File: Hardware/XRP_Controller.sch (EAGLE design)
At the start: 121 parts, among them J1 POWER_JACKPOWER_JACK_SLOT, J12 Vertical Qwiic Connector, J13 Vertical Qwiic Connector, J14 Vertical Qwiic Connector, J3 JST_6_PIN_VERTICAL, J4 JST_6_PIN_VERTICAL, J5 JST_6_PIN_VERTICAL, J6 JST_6_PIN_VERTICAL, J9 Vertical Qwiic Connector, Q3 20V/4.2A/52mΩ/1.4W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

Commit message: Put all XRP specific parts into a single library
Helps ensure PROD_ID values are correct for this project
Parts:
- U1: value RPI_PICO_W -> RPI_PICO_W_XRP; device RPI_PICO_W:RPI_PICO_W -> XRP_COMPONENTS:RPI_PICO_W_XRP
- U4: value LSM6DS0 -> LSM6DS0X; device SparkFun-Sensors:LSM6DSO -> XRP_COMPONENTS:LSM6DSOX_XRP
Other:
- note added: "Cut VUSB jumper to prevent motors and servos from being powered by USB"
- note removed: "Open VUSB jumper to prevent motors and servos from being powered by USB"
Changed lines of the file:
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@@
 <part name="J8" library="SparkFun-Connectors" deviceset="CONN_03" device="LOCK_NO_SILK"/>
 <part name="J9" library="SparkFun-Connectors" deviceset="QWIIC_CONNECTOR" device="" value="Vertical Qwiic Connector"/>
-<part name="U4" library="SparkFun-Sensors" deviceset="LSM6DSO" device="" value="LSM6DS0"/>
+<part name="U4" library="XRP_COMPONENTS" deviceset="LSM6DSOX_XRP" device="" value="LSM6DS0X"/>
 <part name="U5" library="SparkFun-IC-Special-Function" deviceset="DRV883X" device="" value="DRV8835"/>
 <part name="U6" library="SparkFun-IC-Special-Function" deviceset="DRV883X" device="" value="DRV8835"/>
@@
 <part name="R19" library="SparkFun-Resistors" deviceset="10OHM" device="-1206-1/4W-1%" value="10"/>
 <part name="R18" library="SparkFun-Resistors" deviceset="10OHM" device="-1206-1/4W-1%" value="10"/>
-<part name="U1" library="RPI_PICO_W" deviceset="RPI_PICO_W" device=""/>
+<part name="U1" library="XRP_COMPONENTS" deviceset="RPI_PICO_W_XRP" device=""/>
 <part name="TP39" library="SparkFun-Connectors" deviceset="TEST-POINT" device="3X5"/>
 <part name="TP38" library="SparkFun-Connectors" deviceset="TEST-POINT" device="3X5"/>
@@
 <text x="20.32" y="172.72" size="2.54" layer="97" font="vector" align="center">Cut PWR jumper to
 remove power LED</text>
-<text x="45.72" y="93.98" size="2.54" layer="97" font="vector" align="center">Open VUSB jumper to
+<text x="45.72" y="93.98" size="2.54" layer="97" font="vector" align="center">Cut VUSB jumper to
 prevent motors and servos
 from being powered by USB</text>

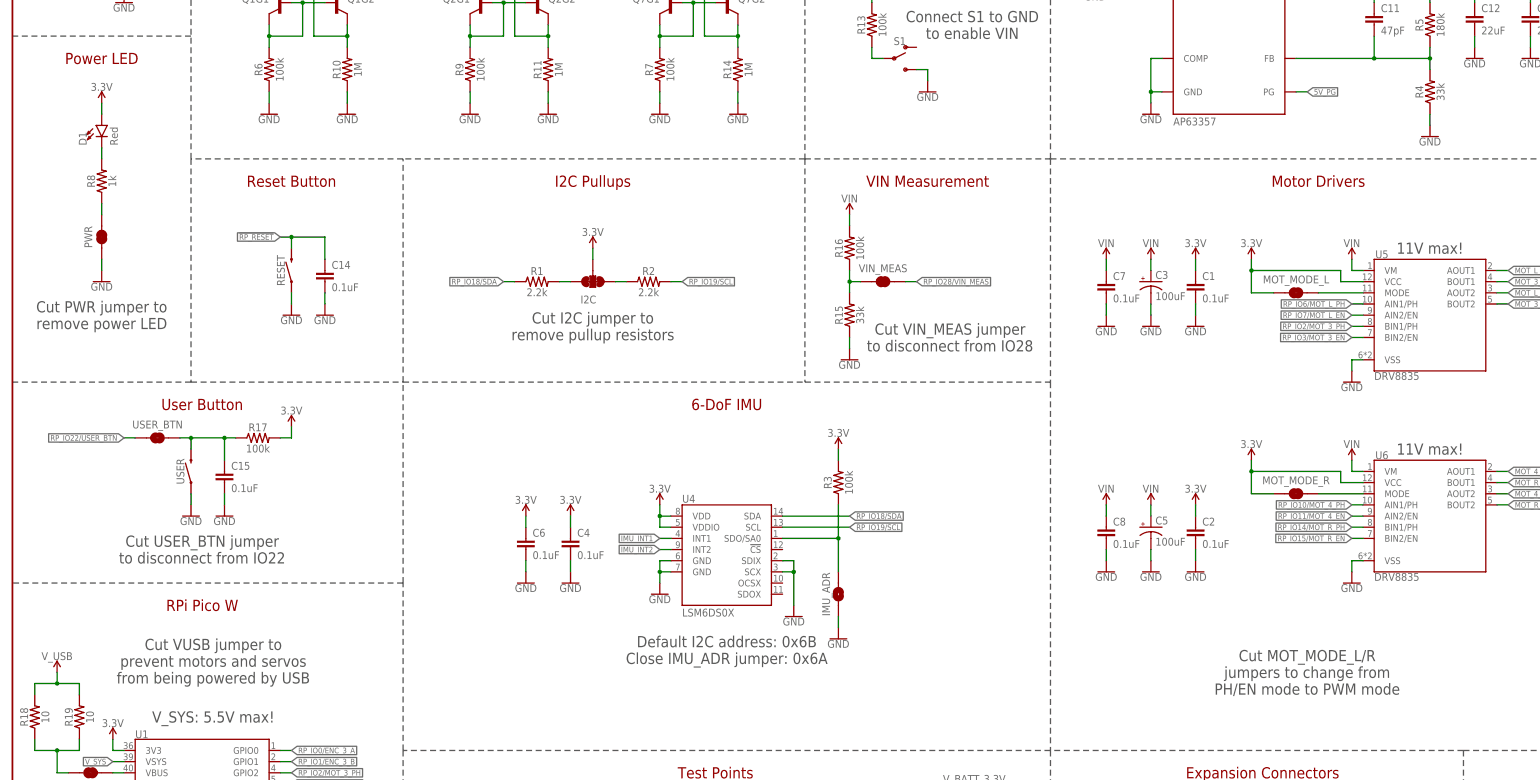
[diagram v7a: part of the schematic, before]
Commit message: Design review updates
Motor mode jumpers - add "/3" and "/4" to jumper names
Overlay copper version number with silk version number
Change IMU_ADR jumper from NO to NC, and swap with R3 to keep same default address
Add second power LED to indicate motor power vs system power
Change power LEDs to DIO-17976 and corresponding resistor values
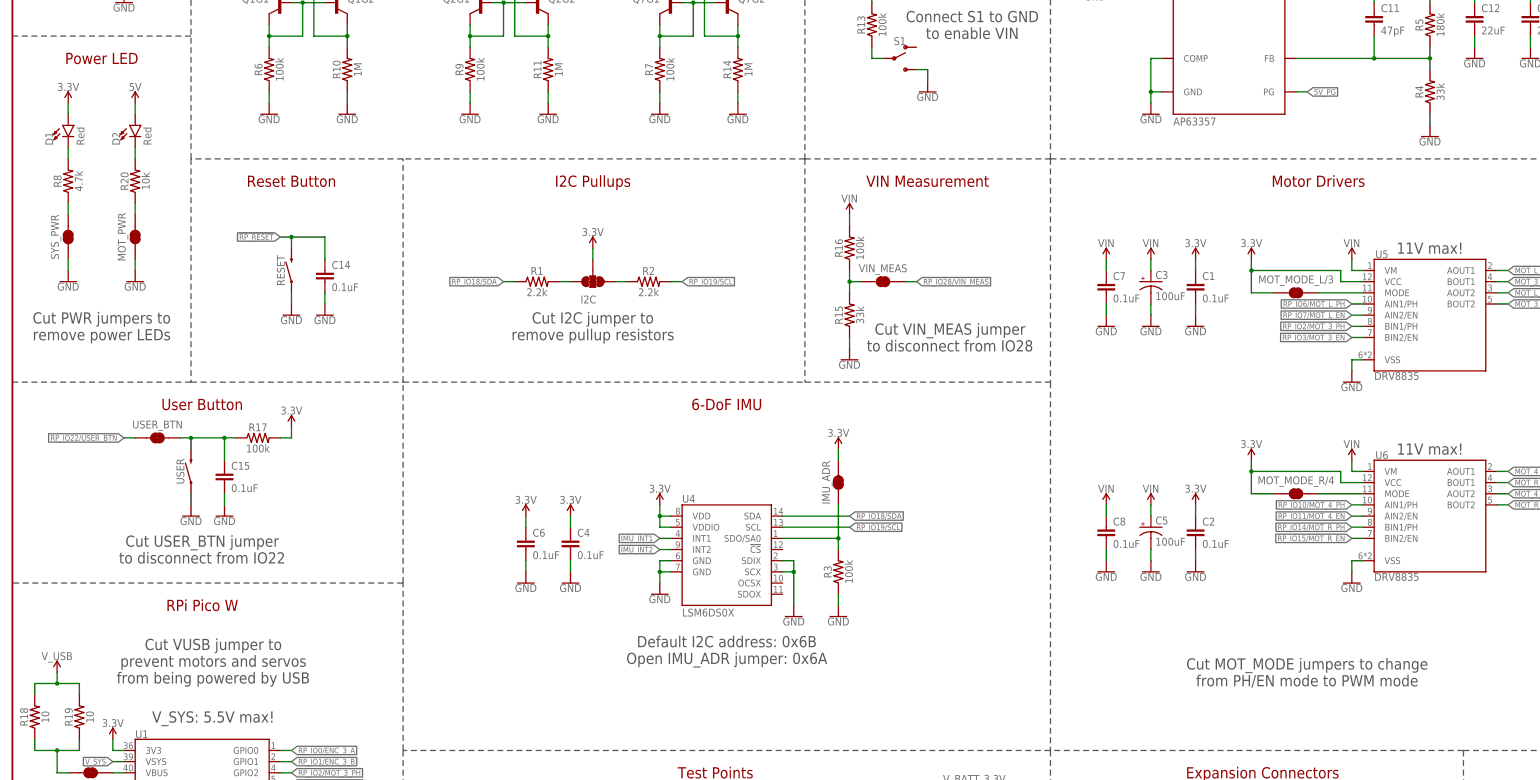
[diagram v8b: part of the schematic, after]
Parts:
- removed PWR: JUMPER-SMT_2_NC_TRACE_SILK, SparkFun-Jumpers:JUMPER-SMT_2_NC_TRACE_SILK
- added D2: Red, SparkFun-LED:LED-RED_0603-KB
- added MOT_PWR, SYS_PWR: JUMPER-SMT_2_NC_TRACE_SILK, SparkFun-Jumpers:JUMPER-SMT_2_NC_TRACE_SILK
- added R20: 10k, SparkFun-Resistors:10KOHM-0603-1/10W-1%
- D1: device SparkFun-LED:LED-RED-0603-WE -> SparkFun-LED:LED-RED_0603-KB
- IMU_ADR: value JUMPER-SMT_2_NO_SILK -> JUMPER-SMT_2_NC_TRACE_SILK; device SparkFun-Jumpers:JUMPER-SMT_2_NO_SILK -> SparkFun-Jumpers:JUMPER-SMT_2_NC_TRACE_SILK
- R8: value 1k -> 4.7k; device SparkFun-Resistors:1KOHM-0603-1/10W-1% -> SparkFun-Resistors:4.7KOHM-0603-1/10W-1%
- renumbered MOT_MODE_L to MOT_MODE_L/3, MOT_MODE_R to MOT_MODE_R/4
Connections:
- new net N$21: D2.C, R20.2
- new net N$22: MOT_PWR.2, R20.1
- net 3.3V: now also IMU_ADR.2; no longer R3.2
- net 5V: now also D2.A
- net GND: now also MOT_PWR.1, R3.1, SYS_PWR.1; no longer IMU_ADR.1, PWR.1
- net N$10: now also SYS_PWR.2; no longer PWR.2
- net N$2: now also IMU_ADR.1, R3.2; no longer IMU_ADR.2, R3.1
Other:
- note added: "Cut MOT_MODE jumpers to change from PH/EN mode to PWM mode"
- note added: "Cut PWR jumpers to remove power LEDs"
- note added: "Default I2C address: 0x6B Open IMU_ADR jumper: 0x6A"
- note removed: "Cut MOT_MODE_L/R jumpers to change from PH/EN mode to PWM mode"
- note removed: "Cut PWR jumper to remove power LED"
- note removed: "Default I2C address: 0x6B Close IMU_ADR jumper: 0x6A"
- moved on the sheet: D1, R3, R8
